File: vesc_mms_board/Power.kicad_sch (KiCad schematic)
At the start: 4 parts, among them J3 VCC_IN, J4 Conn_01x02

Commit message: pcb created
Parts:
- J5: renamed from J3; footprint Connector_AMASS:AMASS_XT60IPW-M_1x03_P7.20mm_Horizontal -> Connector_AMASS:AMASS_XT60PW-M_1x02_P7.20mm_Horizontal
- J6: renamed from J4; footprint (none) -> Connector_PinHeader_2.54mm:PinHeader_1x02_P2.54mm_Vertical
- renumbered H2 to H10, H1 to H9
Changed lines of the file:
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@@
 		(dnp no)
 		(fields_autoplaced yes)
-		(property "Reference" "H1"
+		(property "Reference" "H9"
 			(at 83.82 58.4199 90)
 			(effects
@@
 			(project "vesc_mms_board"
 				(path "/19c3ad7a-1b7d-4298-9053-cf734bfcea10/09185991-2b08-4e41-9e65-0618febadbdd"
-					(reference "H1")
+					(reference "H9")
 					(unit 1)
 				)
@@
 		(on_board yes)
 		(dnp no)
-		(property "Reference" "#PWR015"
+		(property "Reference" "#PWR018"
 			(at 73.66 72.39 0)
 			(effects
@@
 			(project "vesc_mms_board"
 				(path "/19c3ad7a-1b7d-4298-9053-cf734bfcea10/09185991-2b08-4e41-9e65-0618febadbdd"
-					(reference "#PWR015")
+					(reference "#PWR018")
 					(unit 1)
 				)
@@
 		(dnp no)
 		(fields_autoplaced yes)
-		(property "Reference" "J3"
+		(property "Reference" "J5"
 			(at 83.82 40.6399 0)
 			(effects
@@
 			)
 		)
-		(property "Footprint" "Connector_AMASS:AMASS_XT60IPW-M_1x03_P7.20mm_Horizontal"
+		(property "Footprint" "Connector_AMASS:AMASS_XT60PW-M_1x02_P7.20mm_Horizontal"
 			(at 81.28 40.64 0)
 			(effects
@@
 			(project "vesc_mms_board"
 				(path "/19c3ad7a-1b7d-4298-9053-cf734bfcea10/09185991-2b08-4e41-9e65-0618febadbdd"
-					(reference "J3")
+					(reference "J5")
 					(unit 1)
 				)
@@
 		(dnp no)
 		(fields_autoplaced yes)
-		(property "Reference" "J4"
+		(property "Reference" "J6"
 			(at 153.67 49.5299 0)
 			(effects
@@
 			)
 		)
-		(property "Footprint" ""
+		(property "Footprint" "Connector_PinHeader_2.54mm:PinHeader_1x02_P2.54mm_Vertical"
 			(at 151.13 49.53 0)
 			(effects
@@
 			(project "vesc_mms_board"
 				(path "/19c3ad7a-1b7d-4298-9053-cf734bfcea10/09185991-2b08-4e41-9e65-0618febadbdd"
-					(reference "J4")
+					(reference "J6")
 					(unit 1)
 				)
@@
 		(dnp no)
 		(fields_autoplaced yes)
-		(property "Reference" "#PWR014"
+		(property "Reference" "#PWR017"
 			(at 73.66 62.23 0)
 			(effects
@@
 			(project "vesc_mms_board"
 				(path "/19c3ad7a-1b7d-4298-9053-cf734bfcea10/09185991-2b08-4e41-9e65-0618febadbdd"
-					(reference "#PWR014")
+					(reference "#PWR017")
 					(unit 1)
 				)
@@
 		(on_board yes)
 		(dnp no)
-		(property "Reference" "#PWR013"
+		(property "Reference" "#PWR016"
 			(at 72.39 50.8 0)
 			(effects
@@
 			(project "vesc_mms_board"
 				(path "/19c3ad7a-1b7d-4298-9053-cf734bfcea10/09185991-2b08-4e41-9e65-0618febadbdd"
-					(reference "#PWR013")
+					(reference "#PWR016")
 					(unit 1)
 				)
@@
 		(dnp no)
 		(fields_autoplaced yes)
-		(property "Reference" "H2"
+		(property "Reference" "H10"
 			(at 83.82 63.4999 90)
 			(effects
@@
 			(project "vesc_mms_board"
 				(path "/19c3ad7a-1b7d-4298-9053-cf734bfcea10/09185991-2b08-4e41-9e65-0618febadbdd"
-					(reference "H2")
+					(reference "H10")
 					(unit 1)
 				)
@@
 		(dnp no)
 		(fields_autoplaced yes)
-		(property "Reference" "#PWR012"
+		(property "Reference" "#PWR015"
 			(at 72.39 43.18 0)
 			(effects
@@
 			(project "vesc_mms_board"
 				(path "/19c3ad7a-1b7d-4298-9053-cf734bfcea10/09185991-2b08-4e41-9e65-0618febadbdd"
-					(reference "#PWR012")
+					(reference "#PWR015")
 					(unit 1)
 				)
@@
 		(dnp no)
 		(fields_autoplaced yes)
-		(property "Reference" "#PWR018"
+		(property "Reference" "#PWR019"
 			(at 142.24 52.07 0)
 			(effects
@@
 			(project "vesc_mms_board"
 				(path "/19c3ad7a-1b7d-4298-9053-cf734bfcea10/09185991-2b08-4e41-9e65-0618febadbdd"
-					(reference "#PWR018")
+					(reference "#PWR019")
 					(unit 1)
 				)
@@
 		(dnp no)
 		(fields_autoplaced yes)
-		(property "Reference" "#PWR019"
+		(property "Reference" "#PWR020"
 			(at 142.24 60.96 0)
 			(effects
@@
 			(project "vesc_mms_board"
 				(path "/19c3ad7a-1b7d-4298-9053-cf734bfcea10/09185991-2b08-4e41-9e65-0618febadbdd"
-					(reference "#PWR019")
-					(unit 1)
-				)
+					(reference "#PWR020")
+					(unit 1)
+				)

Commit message: updarte readme final desing rev a
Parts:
- added C1: 10u, Capacitor_SMD:C_0603_1608Metric, symbol Device:C
- added C2: 100n, Capacitor_SMD:C_0402_1005Metric, symbol Device:C
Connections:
- net +12V: now also C1.2, C2.2
- net GND: now also C1.1, C2.1
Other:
- moved on the sheet: J6

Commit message: Update rev 2.0, added step files
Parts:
- J6: footprint Connector_PinHeader_2.54mm:PinHeader_1x02_P2.54mm_Vertical -> Connector_JST:JST_XH_B2B-XH-A_1x02_P2.50mm_Vertical
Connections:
- net +12V: now also J6.2 (Pin_2); no longer J6.1 (Pin_1)
- net GND: now also J6.1 (Pin_1); no longer J6.2 (Pin_2)
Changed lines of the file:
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@@
-	)
-	(symbol
-		(lib_id "Connector_Generic:Conn_01x02")
-		(at 151.13 50.8 0)
-		(unit 1)
-		(exclude_from_sim no)
-		(in_bom yes)
-		(on_board yes)
-		(dnp no)
-		(fields_autoplaced yes)
-		(property "Reference" "J6"
-			(at 153.67 50.7999 0)
-			(effects
-				(font
-					(size 1.27 1.27)
-				)
-				(justify left)
-			)
-		)
-		(property "Value" "Conn_01x02"
-			(at 153.67 53.3399 0)
-			(effects
-				(font
-					(size 1.27 1.27)
-				)
-				(justify left)
-			)
-		)
-		(property "Footprint" "Connector_PinHeader_2.54mm:PinHeader_1x02_P2.54mm_Vertical"
-			(at 151.13 50.8 0)
-			(effects
-				(font
-					(size 1.27 1.27)
-				)
-				(hide yes)
-			)
-		)
-		(property "Datasheet" "~"
-			(at 151.13 50.8 0)
-			(effects
-				(font
-					(size 1.27 1.27)
-				)
-				(hide yes)
-			)
-		)
-		(property "Description" "Generic connector, single row, 01x02, script generated (kicad-library-utils/schlib/autogen/connector/)"
-			(at 151.13 50.8 0)
-			(effects
-				(font
-					(size 1.27 1.27)
-				)
-				(hide yes)
-			)
-		)
-		(pin "1"
-		)
-		(pin "2"
-		)
-		(instances
-			(project "vesc_mms_board"
-				(path "/19c3ad7a-1b7d-4298-9053-cf734bfcea10/09185991-2b08-4e41-9e65-0618febadbdd"
-					(reference "J6")
-					(unit 1)
-				)
-			)
-		)
 	)
 	(symbol
@@
 					(unit 1)
 				)
+			)
+		)
+	)
+	(symbol
+		(lib_id "Connector_Generic:Conn_01x02")
+		(at 151.13 53.34 0)
+		(mirror x)
+		(unit 1)
+		(exclude_from_sim no)
+		(in_bom yes)
+		(on_board yes)
+		(dnp no)
+		(property "Reference" "J6"
+			(at 153.67 53.3401 0)
+			(effects
+				(font
+					(size 1.27 1.27)
+				)
+				(justify left)
+			)
+		)
+		(property "Value" "Conn_01x02"
+			(at 153.67 50.8001 0)
+			(effects
+				(font
+					(size 1.27 1.27)
+				)
+				(justify left)
+			)
+		)
+		(property "Footprint" "Connector_JST:JST_XH_B2B-XH-A_1x02_P2.50mm_Vertical"
+			(at 151.13 53.34 0)
+			(effects
+				(font
+					(size 1.27 1.27)
+				)
+				(hide yes)
+			)
+		)
+		(property "Datasheet" "~"
+			(at 151.13 53.34 0)
+			(effects
+				(font
+					(size 1.27 1.27)
+				)
+				(hide yes)
+			)
+		)
+		(property "Description" "Generic connector, single row, 01x02, script generated (kicad-library-utils/schlib/autogen/connector/)"
+			(at 151.13 53.34 0)
+			(effects
+				(font
+					(size 1.27 1.27)
+				)
+				(hide yes)
+			)
+		)
+		(pin "1"
+		)
+		(pin "2"
+		)
+		(instances
+			(project "vesc_mms_board"
+				(path "/19c3ad7a-1b7d-4298-9053-cf734bfcea10/09185991-2b08-4e41-9e65-0618febadbdd"
+					(reference "J6")
+					(unit 1)
+				)

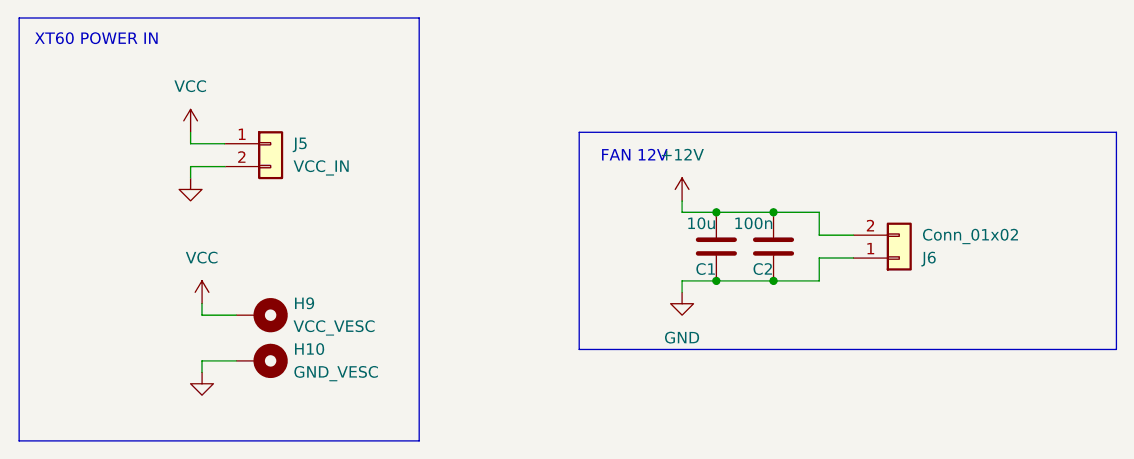
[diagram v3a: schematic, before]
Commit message: fixed problem with xt60
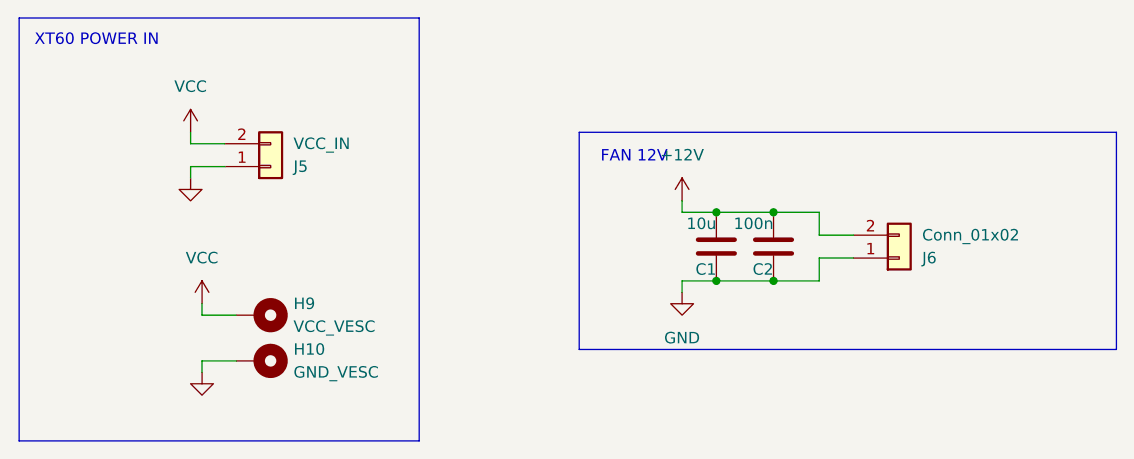
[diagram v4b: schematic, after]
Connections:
- net GND: now also J5.1 (Pin_1); no longer J5.2 (Pin_2)
- net VCC: now also J5.2 (Pin_2); no longer J5.1 (Pin_1)
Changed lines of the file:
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@@
+	(wire
+		(pts
+			(xy 130.81 48.26) (xy 137.16 48.26)
+		)
+		(stroke
+			(width 0)
+			(type default)
+		)
+	)
+	(wire
+		(pts
+			(xy 127 55.88) (xy 127 57.15)
+		)
+		(stroke
+			(width 0)
+			(type default)
+		)
+	)
+	(wire
+		(pts
+			(xy 73.66 58.42) (xy 73.66 59.69)
+		)
+		(stroke
+			(width 0)
+			(type default)
+		)
+	)
+	(wire
+		(pts
+			(xy 73.66 64.77) (xy 77.47 64.77)
+		)
+		(stroke
+			(width 0)
+			(type default)
+		)
+	)
+	(wire
+		(pts
+			(xy 142.24 50.8) (xy 146.05 50.8)
+		)
+		(stroke
+			(width 0)
+			(type default)
+		)
+	)
+	(wire
+		(pts
+			(xy 72.39 43.18) (xy 76.2 43.18)
+		)
+		(stroke
+			(width 0)
+			(type default)
+		)
+	)
+	(wire
+		(pts
+			(xy 127 46.99) (xy 127 48.26)
+		)
+		(stroke
+			(width 0)
+			(type default)
+		)
+	)
 	(wire
 		(pts
 			(xy 72.39 40.64) (xy 76.2 40.64)
-		)
-		(stroke
-			(width 0)
-			(type default)
-		)
-	)
-	(wire
-		(pts
-			(xy 130.81 48.26) (xy 137.16 48.26)
-		)
-		(stroke
-			(width 0)
-			(type default)
-		)
-	)
-	(wire
-		(pts
-			(xy 127 55.88) (xy 127 57.15)
-		)
-		(stroke
-			(width 0)
-			(type default)
-		)
-	)
-	(wire
-		(pts
-			(xy 73.66 58.42) (xy 73.66 59.69)
-		)
-		(stroke
-			(width 0)
-			(type default)
-		)
-	)
-	(wire
-		(pts
-			(xy 73.66 64.77) (xy 77.47 64.77)
-		)
-		(stroke
-			(width 0)
-			(type default)
-		)
-	)
-	(wire
-		(pts
-			(xy 142.24 50.8) (xy 146.05 50.8)
-		)
-		(stroke
-			(width 0)
-			(type default)
-		)
-	)
-	(wire
-		(pts
-			(xy 72.39 43.18) (xy 76.2 43.18)
-		)
-		(stroke
-			(width 0)
-			(type default)
-		)
-	)
-	(wire
-		(pts
-			(xy 127 46.99) (xy 127 48.26)
 		)
 		(stroke
@@
 	(symbol
 		(lib_id "Connector_Generic:Conn_01x02")
-		(at 81.28 40.64 0)
+		(at 81.28 43.18 0)
+		(mirror x)
 		(unit 1)
 		(exclude_from_sim no)
@@
 		(on_board yes)
 		(dnp no)
-		(fields_autoplaced yes)
 		(property "Reference" "J5"
-			(at 83.82 40.6399 0)
+			(at 83.82 43.1801 0)
 			(effects
 				(font
@@
 		)
 		(property "Value" "VCC_IN"
-			(at 83.82 43.1799 0)
+			(at 83.82 40.6401 0)
 			(effects
 				(font
@@
 		)
 		(property "Footprint" "Connector_AMASS:AMASS_XT60PW-M_1x02_P7.20mm_Horizontal"
-			(at 81.28 40.64 0)
+			(at 81.28 43.18 0)
 			(effects
 				(font
@@
 		)
 		(property "Datasheet" "~"
-			(at 81.28 40.64 0)
+			(at 81.28 43.18 0)
 			(effects
 				(font
@@
 		)
 		(property "Description" "Generic connector, single row, 01x02, script generated (kicad-library-utils/schlib/autogen/connector/)"
-			(at 81.28 40.64 0)
-			(effects
-				(font
+			(at 81.28 43.18 0)
+			(effects
+				(font
